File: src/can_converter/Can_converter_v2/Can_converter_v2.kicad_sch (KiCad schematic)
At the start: 10 parts, among them J1 SM02B-PASS, X1 629722000214_pasteInHole

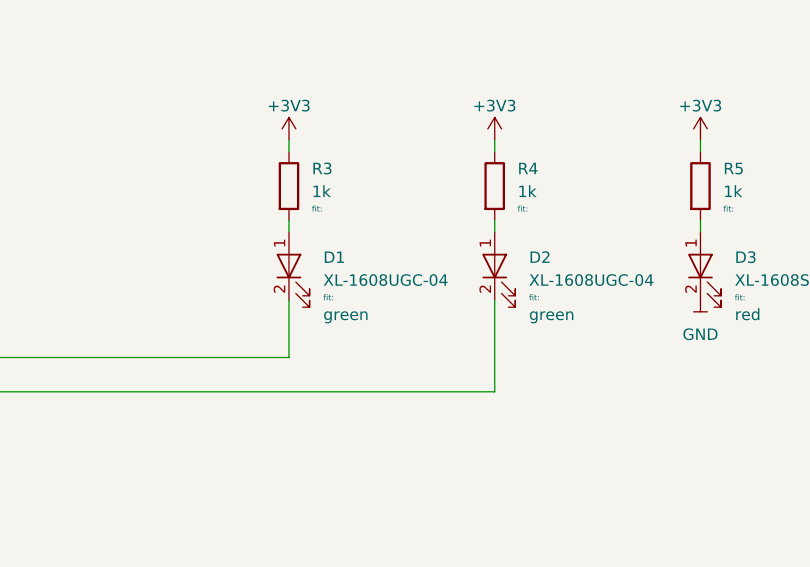
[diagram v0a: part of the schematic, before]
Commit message: Rebase usb-can branch onto main
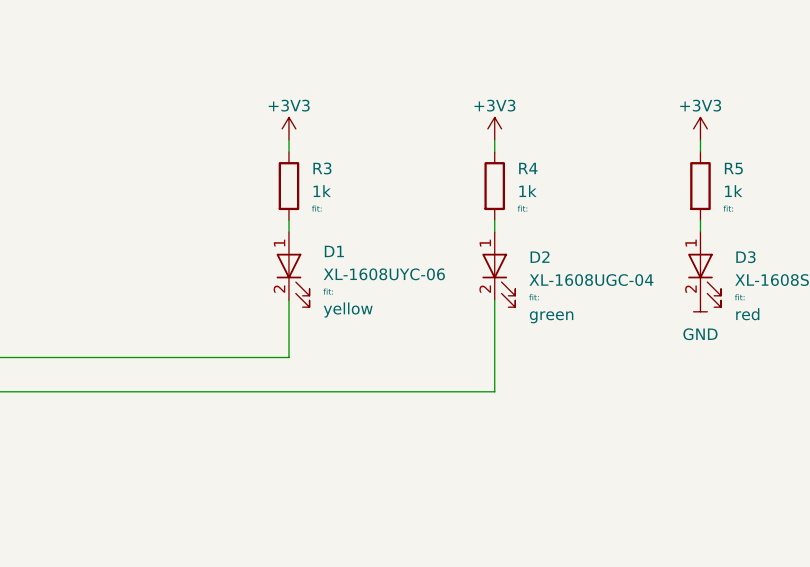
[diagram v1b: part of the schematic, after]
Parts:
- D1: value XL-1608UGC-04 -> XL-1608UYC-06; color green -> yellow
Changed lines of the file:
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@@
 		(fields_autoplaced yes)
 		(property "Reference" "D1"
-			(at 210.82 127.3302 90)
-			(effects
-				(font
-					(size 1.27 1.27)
-				)
-				(justify right)
-			)
-		)
-		(property "Value" "XL-1608UGC-04"
-			(at 210.82 129.8702 90)
+			(at 210.82 126.6951 90)
+			(effects
+				(font
+					(size 1.27 1.27)
+				)
+				(justify right)
+			)
+		)
+		(property "Value" "XL-1608UYC-06"
+			(at 210.82 129.2351 90)
 			(effects
 				(font
@@
 		)
 		(property "Fit" "fit: "
-			(at 210.82 131.7752 90)
+			(at 210.82 131.1402 90)
 			(effects
 				(font
@@
 			)
 		)
-		(property "color" "green"
-			(at 210.82 133.6802 90)
+		(property "color" "yellow"
+			(at 210.82 133.0451 90)
 			(effects
 				(font
@@
 		)
 		(instances
-			(project "Can_converter_v1"
+			(project "Can_converter_v2"
 				(path "/e63e39d7-6ac0-4ffd-8aa3-1841a4541b55"
 					(page "3")
@@
 		)
 		(instances
-			(project "Can_converter_v1"
+			(project "Can_converter_v2"
 				(path "/e63e39d7-6ac0-4ffd-8aa3-1841a4541b55"
 					(page "4")
@@
 		)
 		(instances
-			(project "Can_converter_v1"
+			(project "Can_converter_v2"
 				(path "/e63e39d7-6ac0-4ffd-8aa3-1841a4541b55"
 					(page "2")
